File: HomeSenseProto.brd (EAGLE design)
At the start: 44 x 44 mm, 24 parts, among them IC1 ESP12SMT

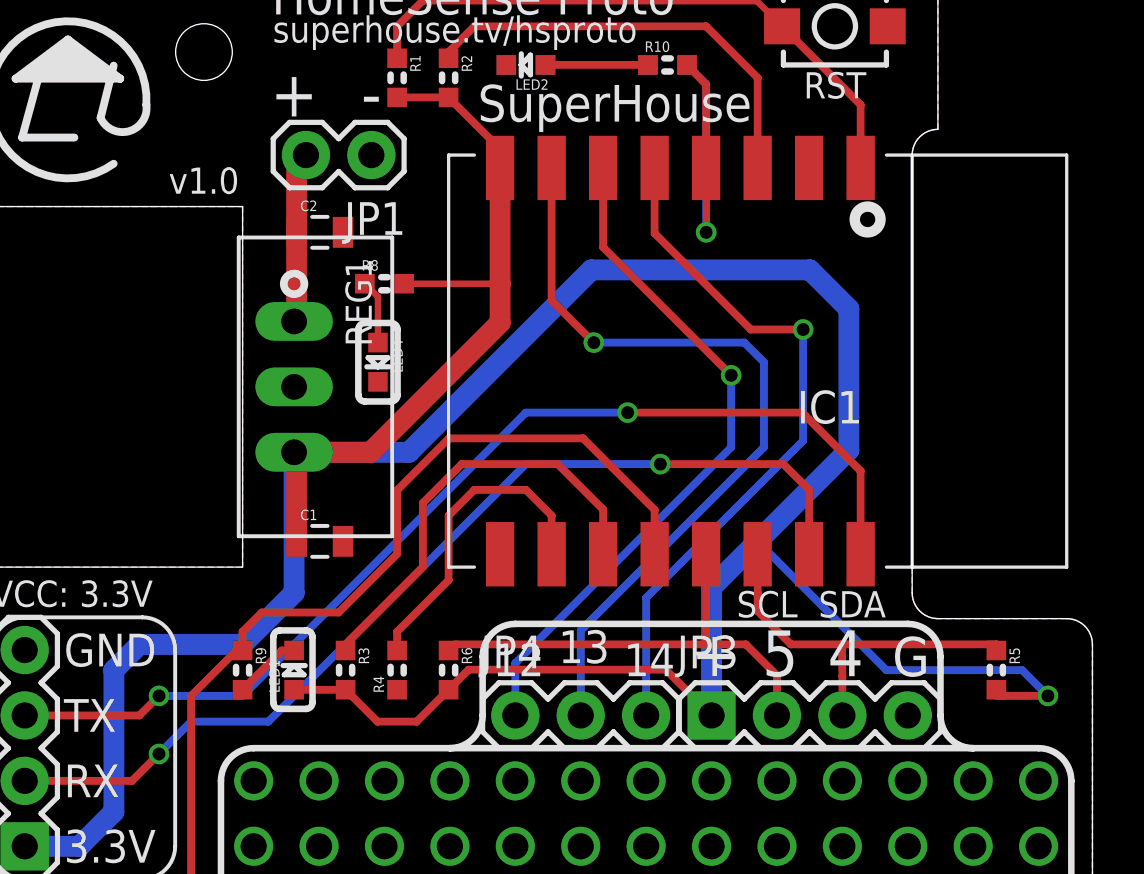
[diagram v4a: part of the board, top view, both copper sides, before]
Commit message: Fixed footprint for ESP12 with correct GPIO4/5
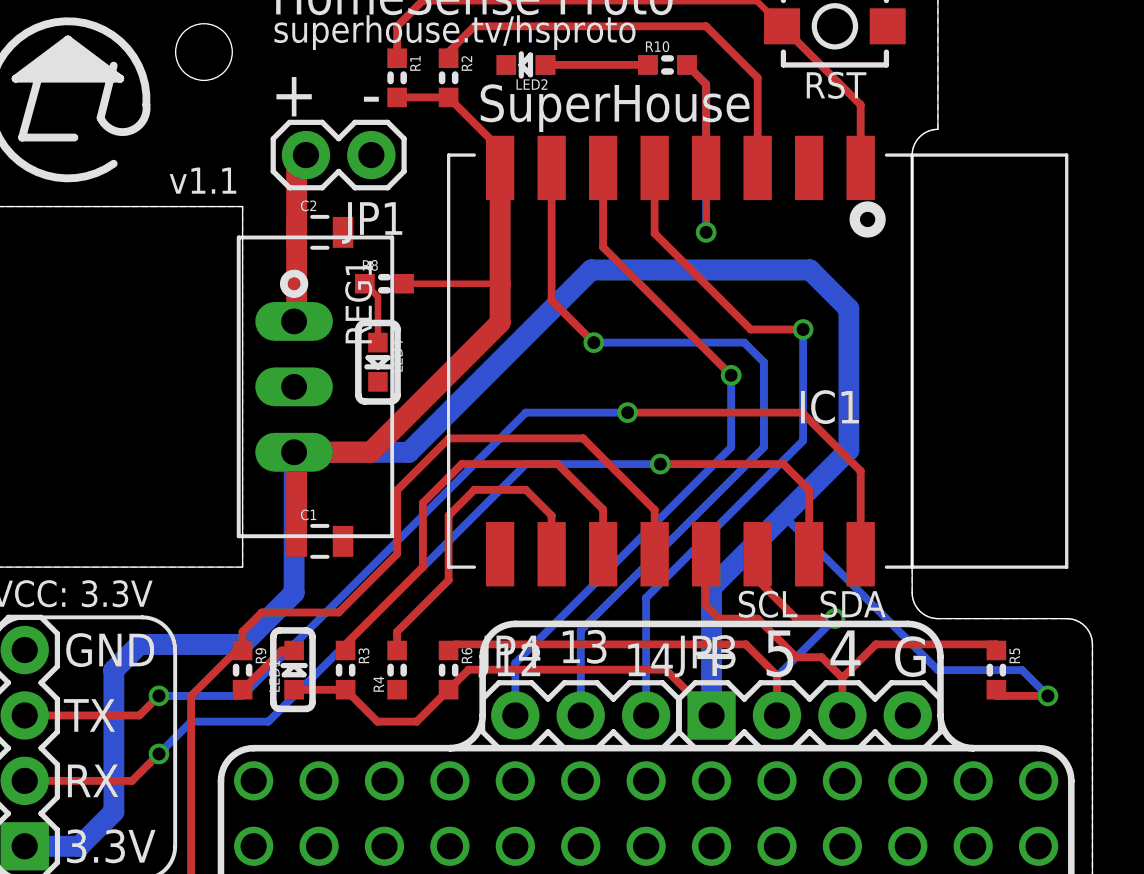
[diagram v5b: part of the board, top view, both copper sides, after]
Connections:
- net GPIO4: now also IC1.13; no longer IC1.14
- net GPIO5: now also IC1.14; no longer IC1.13
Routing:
- net GPIO5: track 18.4 -> 24.3 mm, vias 0 -> 1
- net GPIO4: track 15.0 -> 16.7 mm
- net 3.3V: track 129.5 -> 128.9 mm
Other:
- board text added: "v1.1"
- board text removed: "v1.0"
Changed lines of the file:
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@@
 <?xml version="1.0" encoding="utf-8"?>
 <!DOCTYPE eagle SYSTEM "eagle.dtd">
-<eagle version="8.6.0">
+<eagle version="8.7.0">
 <drawing>
 <settings>
@@
 <setting verticaltext="up"/>
 </settings>
-<grid distance="0.01" unitdist="inch" unit="inch" style="lines" multiple="1" display="yes" altdistance="5" altunitdist="mil" altunit="mil"/>
+<grid distance="0.5" unitdist="mm" unit="mm" style="lines" multiple="1" display="yes" altdistance="5" altunitdist="mil" altunit="mil"/>
 <layers>
 <layer number="1" name="Top" color="4" fill="1" visible="yes" active="yes"/>
@@
 <layer number="20" name="Dimension" color="15" fill="1" visible="yes" active="yes"/>
 <layer number="21" name="tPlace" color="15" fill="1" visible="yes" active="yes"/>
-<layer number="22" name="bPlace" color="14" fill="1" visible="yes" active="yes"/>
+<layer number="22" name="bPlace" color="14" fill="1" visible="no" active="yes"/>
 <layer number="23" name="tOrigins" color="15" fill="1" visible="yes" active="yes"/>
 <layer number="24" name="bOrigins" color="3" fill="1" visible="yes" active="yes"/>
@@
 <text x="16" y="38.5" size="1.778" layer="21" font="vector" ratio="18" align="bottom-center">-</text>
 <text x="20.13" y="38.3" size="1.4224" layer="21" font="vector" ratio="18">SuperHouse</text>
-<text x="9.5" y="35.5" size="1.016" layer="21" font="vector" ratio="18" align="bottom-center">v1.0</text>
+<text x="9.5" y="35.5" size="1.016" layer="21" font="vector" ratio="18" align="bottom-center">v1.1</text>
 <wire x1="39.37" y1="13.97" x2="41.91" y2="13.97" width="0.254" layer="22"/>
 <wire x1="41.91" y1="13.97" x2="43.18" y2="12.7" width="0.254" layer="22" curve="-90"/>
@@
 </signal>
 <signal name="GPIO4">
-<contactref element="IC1" pad="14"/>
+<contactref element="IC1" pad="13"/>
 <contactref element="R5" pad="1"/>
 <contactref element="JP3" pad="3"/>
 <wire x1="40.27" y1="17.762" x2="40.27" y2="18" width="0.3048" layer="1"/>
-<wire x1="34.27" y1="18" x2="34.29" y2="16.75" width="0.3048" layer="1"/>
-<wire x1="34.29" y1="16.75" x2="34.29" y2="15.24" width="0.3048" layer="1"/>
-<wire x1="40.27" y1="18" x2="34.27" y2="18" width="0.3048" layer="1"/>
-<wire x1="31" y1="20" x2="31" y2="21.5" width="0.3048" layer="1"/>
-<wire x1="34.27" y1="18" x2="32.292" y2="18" width="0.3048" layer="1"/>
-<wire x1="31" y1="19.292" x2="31" y2="20" width="0.3048" layer="1"/>
-<wire x1="32.292" y1="18" x2="31" y2="19.292" width="0.3048" layer="1"/>
+<wire x1="40.27" y1="18" x2="35.594" y2="18" width="0.3048" layer="1"/>
+<wire x1="35.594" y1="18" x2="34.29" y2="16.696" width="0.3048" layer="1"/>
+<wire x1="34.29" y1="16.696" x2="34.29" y2="15.24" width="0.3048" layer="1"/>
+<wire x1="34.29" y1="16.696" x2="33.486" y2="17.5" width="0.3048" layer="1"/>
+<wire x1="33.486" y1="17.5" x2="32.5" y2="17.5" width="0.3048" layer="1"/>
+<wire x1="32.5" y1="17.5" x2="31" y2="19" width="0.3048" layer="1"/>
+<wire x1="31" y1="19" x2="29.5" y2="19" width="0.3048" layer="1"/>
+<wire x1="29.5" y1="19" x2="29" y2="19.5" width="0.3048" layer="1"/>
+<wire x1="29" y1="19.5" x2="29" y2="21.5" width="0.3048" layer="1"/>
 </signal>
 <signal name="GPIO5">
-<contactref element="IC1" pad="13"/>
+<contactref element="IC1" pad="14"/>
 <contactref element="R6" pad="1"/>
 <contactref element="JP3" pad="2"/>
@@
 <wire x1="19.238" y1="18" x2="28.956" y2="18" width="0.3048" layer="1"/>
 <wire x1="28.956" y1="18" x2="30.54" y2="18" width="0.3048" layer="1"/>
+<wire x1="29" y1="18.044" x2="28.956" y2="18" width="0.254" layer="1"/>
 <wire x1="30.54" y1="18" x2="31.75" y2="16.79" width="0.3048" layer="1"/>
 <wire x1="31.75" y1="16.79" x2="31.75" y2="15.24" width="0.3048" layer="1"/>
-<wire x1="29" y1="21.5" x2="29" y2="18.044" width="0.3048" layer="1"/>
-<wire x1="29" y1="18.044" x2="28.956" y2="18" width="0.254" layer="1"/>
+<wire x1="34" y1="19" x2="32.5" y2="19" width="0.3048" layer="1"/>
+<via x="34" y="19" extent="1-16" drill="0.5"/>
+<wire x1="34" y1="19" x2="31.75" y2="16.75" width="0.3048" layer="16"/>
+<wire x1="31.75" y1="16.75" x2="31.75" y2="15.24" width="0.3048" layer="16"/>
+<wire x1="31" y1="20.5" x2="31" y2="21.5" width="0.3048" layer="1"/>
+<wire x1="32.5" y1="19" x2="31" y2="20.5" width="0.3048" layer="1"/>
 </signal>
 <signal name="GPIO0">
@@
 <wire x1="34.54" y1="31.032" x2="34.54" y2="25.54" width="0.8128" layer="16"/>
 <wire x1="29.21" y1="20.21" x2="29.21" y2="15.24" width="0.8128" layer="16"/>
-<wire x1="34.54" y1="25.54" x2="31" y2="22" width="0.8128" layer="16"/>
-<wire x1="31" y1="22" x2="29.21" y2="20.21" width="0.8128" layer="16"/>
-<wire x1="41.27" y1="17" x2="36" y2="17" width="0.3048" layer="16"/>
-<wire x1="36" y1="17" x2="31" y2="22" width="0.3048" layer="16"/>
+<wire x1="34.54" y1="25.54" x2="32" y2="23" width="0.8128" layer="16"/>
+<wire x1="32" y1="23" x2="29.21" y2="20.21" width="0.8128" layer="16"/>
+<wire x1="41.27" y1="17" x2="38" y2="17" width="0.3048" layer="16"/>
+<wire x1="38" y1="17" x2="32" y2="23" width="0.3048" layer="16"/>
 <wire x1="19.78" y1="17.018" x2="19" y2="16.238" width="0.3048" layer="1"/>
 <wire x1="29.21" y1="15.24" x2="27.432" y2="17.018" width="0.3048" layer="1"/>
